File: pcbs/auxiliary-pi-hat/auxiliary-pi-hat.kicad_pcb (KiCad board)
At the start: 2 copper layers, 85 x 56 mm, 29 parts, among them J1 Conn_01x02, J10 Conn_01x03, J11 Conn_01x03, J2 Raspberry Pi - Hat Template -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, J3 Conn_01x03, J4 Conn_01x03, J5 Conn_01x03, J7 Conn_01x04, J8 Conn_02x04_Odd_Even, J9 Conn_01x05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

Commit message: PCB update
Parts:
- added JP1: Jumper_3_Open, Jumper:SolderJumper-3_P1.3mm_Open_Pad1.0x1.5mm, F.Cu at (145.2, 81.0)
- added R10: 10k, Resistor_SMD:R_1206_3216Metric, F.Cu at (162.2, 61.0)
- added R11: 10k, Resistor_SMD:R_1206_3216Metric, F.Cu at (165.8, 61.0)
- added R12: 10k, Resistor_SMD:R_1206_3216Metric, F.Cu at (169.0, 61.0)
- J2: footprint General:Raspberry Pi - Hat Template - Full Size -> sbcs:Raspberry Pi - Hat Template - Full Size Extended
- MOD1: footprint General:BNO055 Module -> general:BNO055 Module; moved to B.Cu
- R4: value R_Small_US -> 10k
- U1: footprint MCU_Modules:YAAJ_WeAct_BlackPill_2 -> mcus:Blackpill WeAct
- moved G*** 132.1 mm to (97.2, 75.5)
- moved LS1 83.5 mm to (98.8, 92.5), turned to 0 degrees
- moved SW1 72.0 mm to (90.8, 89.0), turned to -90 degrees
- moved Q3 62.0 mm to (107.5, 88.8)
- moved U2 61.1 mm to (132.9, 60.9), turned to -90 degrees
- moved R4 51.2 mm to (159.0, 61.0)
- moved R1 46.1 mm to (127.5, 64.0), turned to 180 degrees
- moved J11 44.2 mm to (99.0, 59.2), turned to 180 degrees
- moved J1 42.0 mm to (88.2, 55.8), turned to -90 degrees
- moved J3 32.8 mm to (165.0, 98.5)
- moved R2 31.9 mm to (139.0, 81.2), turned to 0 degrees
- moved R3 30.7 mm to (162.5, 89.5)
- moved R5 28.8 mm to (162.5, 74.0), turned to 90 degrees
- moved R6 28.4 mm to (162.5, 79.5)
- moved J10 26.5 mm to (171.5, 98.5)
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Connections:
- J2 pad 17: unconnected-(J2-3.3v-Pad17) -> 3v3-RPI
- J2 pad 32: BUZZER -> BUZZER_RPI
- J4 pad 2: GPIO-2 -> AUX
- R2 pad 2: BUZZER -> Net-(JP1-C)
- R4 pad 1: NEO-1 -> GPIO-20
- R4 pad 2: Net-(J4-Pin_2) -> 3v3-RPI
- U1 pad 16: BTN-1 -> AUX
- U1 pad 17: unconnected-(U1-PB9-Pad17) -> BUZZER_MCU
- U1 pad 23: unconnected-(U1-PC14-Pad23) -> BTN-1
- U1 pad 27: RC-PWM-0 -> unconnected-(U1-PA1-Pad27)
- U1 pad 5: unconnected-(U1-PA8-Pad5) -> RC-PWM-0
- U2 pad 5: +5V -> +3.3V
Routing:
- net +3.3V: track 0.00 -> 210.4 mm, vias 0 -> 4
- net +5V: track 0.00 -> 202.6 mm, vias 0 -> 2
- net GND: track 0.00 -> 108.0 mm, vias 0 -> 7
- net TFT-CS: track 0.00 -> 89.2 mm, vias 0 -> 2
- net TFT-RESET: track 0.00 -> 84.2 mm, vias 0 -> 2
- net TFT-DC: track 0.00 -> 80.4 mm, vias 0 -> 2
- net TFT-MOSI: track 0.00 -> 76.4 mm, vias 0 -> 2
- net BTN-1: track 0.00 -> 75.0 mm
- net TFT-SCK: track 0.00 -> 70.4 mm, vias 0 -> 2
- net SDA: track 0.00 -> 65.7 mm, vias 0 -> 2
- net SCL: track 0.00 -> 65.6 mm, vias 0 -> 2
- net NEO-0: track 0.00 -> 64.7 mm, vias 0 -> 2
- net RC-PWM-0: track 0.00 -> 55.7 mm
- net NEO-1: track 0.00 -> 54.5 mm
- net 3v3-RPI: track 0.00 -> 53.9 mm
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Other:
- board size 85 x 56 mm -> 93 x 56 mm
- board text added: "CONTACTS"
- board text added: "ElectroPup Auxiliary Pi Hat metaphasiclabs.com 10/2024"
- board text added: "SKY"
- board text added: "STM32 Blackpill"
- board text removed: "BTN0"
- board text removed: "BTN1"
- board text removed: "ElectroPup Auxiliary Pi Hat metaphasiclabs.com 09/2024"
- board text removed: "STM32 Bluepill/Blackpill"

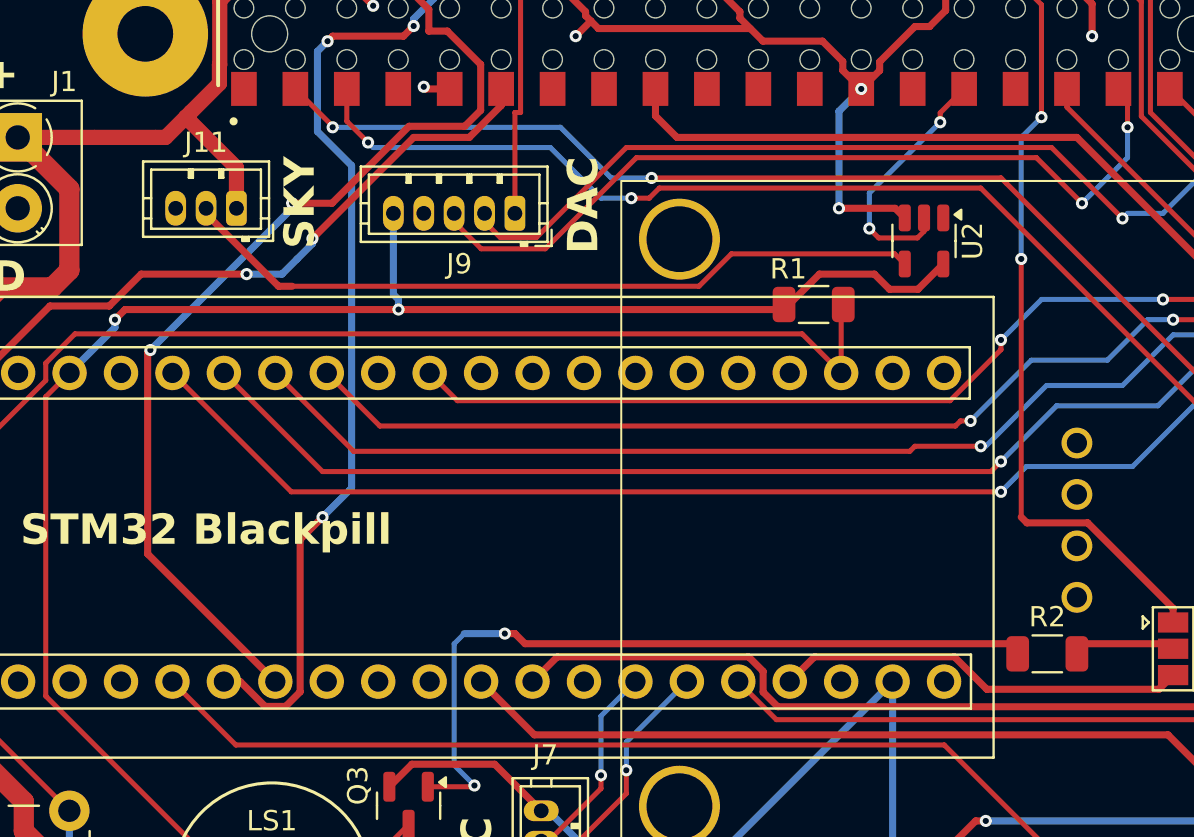
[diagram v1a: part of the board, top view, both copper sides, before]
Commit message: plot.py update to handle no gamepad connected
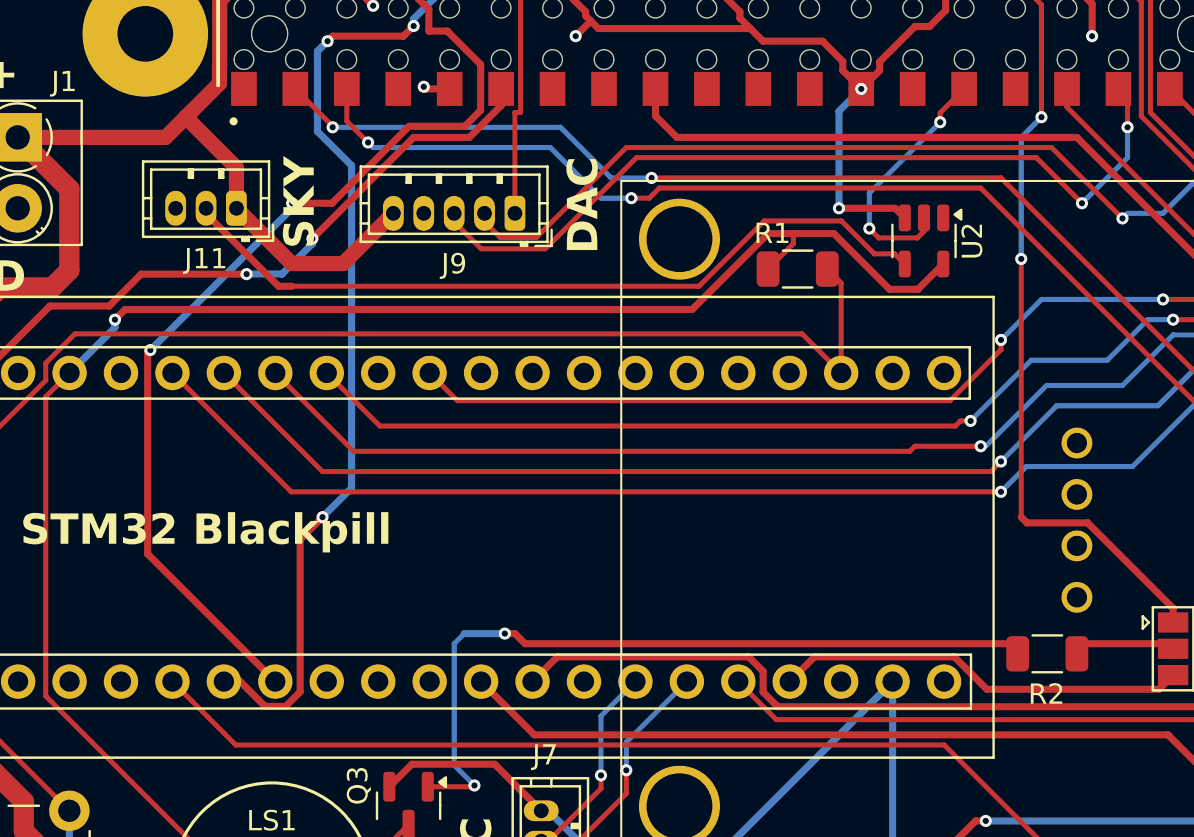
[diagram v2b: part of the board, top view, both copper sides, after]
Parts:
- moved R1 1.92 mm to (126.7, 62.2)
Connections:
- J9 pad 5: +3.3V -> +5V
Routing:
- net +5V: track 202.6 -> 212.5 mm
- net BTN-1: track 75.0 -> 77.3 mm
- net Net-(J11-Pin_2): track 37.4 -> 38.7 mm
- net +3.3V: track 210.4 -> 209.4 mm, vias 4 -> 3
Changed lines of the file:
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@@
 		(tags "resistor")
 		(property "Reference" "R2"
-			(at 0 -1.82 360)
+			(at -0.0375 2 360)
 			(layer "F.SilkS")
 			(effects
@@
 		(tags "connector JST ZH vertical")
 		(property "Reference" "J9"
-			(at 2.75 -2.5 180)
+			(at 3 -2.5 180)
 			(layer "F.SilkS")
 			(effects
@@
 			(layers "*.Cu" "*.Mask")
 			(remove_unused_layers no)
-			(net 14 "+3.3V")
+			(net 7 "+5V")
 			(pinfunction "Pin_5")
 			(pintype "passive")
@@
 		(tags "connector JST ZH vertical")
 		(property "Reference" "J11"
-			(at 1.5 3.25 360)
+			(at 1.5 -2.5 360)
 			(layer "F.SilkS")
 			(effects
@@
 	(footprint "Resistor_SMD:R_1206_3216Metric"
 		(layer "F.Cu")
-		(at 127.5 64 180)
+		(at 126.7125 62.25 180)
 		(descr "Resistor SMD 1206 (3216 Metric), square (rectangular) end terminal, IPC_7351 nominal, (Body size source: IPC-SM-782 page 72, https://www.pcb-3d.com/wordpress/wp-content/uploads/ipc-sm-782a_amendment_1_and_2.pdf), generated with kicad-footprint-generator")
 		(tags "resistor")
@@
 	)
 	(segment
+		(start 104.269925 61.980075)
+		(end 101.730075 61.980075)
+		(width 0.75)
+		(layer "F.Cu")
+		(net 7)
+	)
+	(segment
 		(start 88.5 90)
 		(end 88.5 88.54)
@@
 	)
 	(segment
+		(start 101.730075 61.980075)
+		(end 99 59.25)
+		(width 0.75)
+		(layer "F.Cu")
+		(net 7)
+	)
+	(segment
+		(start 106.75 59.5)
+		(end 104.269925 61.980075)
+		(width 0.75)
+		(layer "F.Cu")
+		(net 7)
+	)
+	(segment
 		(start 90.75 58.3)
 		(end 88.2 55.75)
@@
 	)
 	(segment
-		(start 127.7875 62.5)
-		(end 126.0375 64.25)
-		(width 0.35)
-		(layer "F.Cu")
-		(net 14)
-	)
-	(segment
 		(start 163.75 88.75)
 		(end 163 89.5)
@@
 	)
 	(segment
-		(start 131.25 63.25)
-		(end 130.5 62.5)
-		(width 0.35)
-		(layer "F.Cu")
-		(net 14)
-	)
-	(segment
 		(start 163.75 83.8625)
 		(end 163.75 88.75)
@@
 	)
 	(segment
-		(start 126.0375 64.25)
-		(end 107 64.25)
-		(width 0.35)
-		(layer "F.Cu")
-		(net 14)
-	)
-	(segment
 		(start 163.9625 83.05)
 		(end 163.45 83.5625)
@@
 	)
 	(segment
-		(start 93.5 64.25)
-		(end 93 64.75)
-		(width 0.35)
-		(layer "F.Cu")
-		(net 14)
-	)
-	(segment
 		(start 169.4625 74.9625)
 		(end 169.025 74.525)
@@
 	)
 	(segment
-		(start 130.5 62.5)
-		(end 127.7875 62.5)
+		(start 93.5 64.25)
+		(end 93 64.75)
 		(width 0.35)
 		(layer "F.Cu")
@@
 	)
 	(segment
+		(start 125.25 62.25)
+		(end 126.5 61)
+		(width 0.25)
+		(layer "F.Cu")
+		(net 14)
+	)
+	(segment
 		(start 175.137 67.147)
 		(end 175.137 82.653)
@@
 	)
 	(segment
+		(start 133.9 62)
+		(end 132.65 63.25)
+		(width 0.35)
+		(layer "F.Cu")
+		(net 14)
+	)
+	(segment
+		(start 132.65 63.25)
+		(end 131.25 63.25)
+		(width 0.35)
+		(layer "F.Cu")
+		(net 14)
+	)
+	(segment
 		(start 160.5 89.5)
 		(end 152.5 89.5)
@@
 	)
 	(segment
+		(start 126.5 61)
+		(end 126.5 60.5)
+		(width 0.25)
+		(layer "F.Cu")
+		(net 14)
+	)
+	(segment
 		(start 169.025 74.525)
 		(end 166.975 74.525)
@@
 	)
 	(segment
-		(start 132.65 63.25)
-		(end 131.25 63.25)
+		(start 131.25 63.25)
+		(end 128.5 60.5)
 		(width 0.35)
 		(layer "F.Cu")
@@
 	)
 	(segment
-		(start 174 66.01)
-		(end 175.137 67.147)
+		(start 126.5 60.5)
+		(end 125.25 60.5)
 		(width 0.35)
 		(layer "F.Cu")
@@
 	)
 	(segment
-		(start 133.9 62)
-		(end 132.65 63.25)
+		(start 174 66.01)
+		(end 175.137 67.147)
 		(width 0.35)
 		(layer "F.Cu")
@@
 	)
 	(segment
+		(start 125.25 60.5)
+		(end 121.5 64.25)
+		(width 0.35)
+		(layer "F.Cu")
+		(net 14)
+	)
+	(segment
 		(start 159.365 98.5)
 		(end 158.5 98.5)
@@
 	)
 	(segment
-		(start 107 64.25)
+		(start 121.5 64.25)
 		(end 93.5 64.25)
 		(width 0.35)
@@
 	)
 	(segment
+		(start 128.5 60.5)
+		(end 126.5 60.5)
+		(width 0.35)
+		(layer "F.Cu")
+		(net 14)
+	)
+	(segment
 		(start 163 89.5)
 		(end 160.5 89.5)
@@
 		(net 14)
 	)
-	(via
-		(at 107 64.25)
-		(size 0.6)
-		(drill 0.3)
-		(layers "F.Cu" "B.Cu")
-		(net 14)
-	)
 	(segment
 		(start 152.5 89.5)
@@
 	)
 	(segment
-		(start 107 63.75)
-		(end 106.75 63.5)
-		(width 0.35)
-		(layer "B.Cu")
-		(net 14)
-	)
-	(segment
-		(start 106.75 63.5)
-		(end 106.75 59.5)
-		(width 0.35)
-		(layer "B.Cu")
-		(net 14)
-	)
-	(segment
-		(start 107 64.25)
-		(end 107 63.75)
-		(width 0.35)
-		(layer "B.Cu")
-		(net 14)
-	)
-	(segment
 		(start 93 64.75)
 		(end 93 65.14)
@@
 	)
 	(segment
-		(start 90.75 89)
-		(end 87.045 85.295)
+		(start 128.86 62.935)
+		(end 128.175 62.25)
 		(width 0.25)
 		(layer "F.Cu")
@@
 	)
 	(segment
-		(start 87.045 85.295)
-		(end 87.045 70.29)
+		(start 128.86 67.38)
+		(end 128.86 62.935)
 		(width 0.25)
 		(layer "F.Cu")
@@
 	)
 	(segment
-		(start 91.028299 65.45)
-		(end 126.93 65.45)
+		(start 90.75 89)
+		(end 87.045 85.295)
 		(width 0.25)
 		(layer "F.Cu")
@@
 	)
 	(segment
-		(start 128.86 64.3525)
-		(end 128.9625 64.25)
+		(start 87.045 85.295)
+		(end 87.045 70.29)
 		(width 0.25)
 		(layer "F.Cu")
@@
 	)
 	(segment
-		(start 128.86 67.38)
-		(end 128.86 64.3525)
+		(start 91.028299 65.45)
+		(end 126.93 65.45)
 		(width 0.25)
 		(layer "F.Cu")
@@
 	)
 	(segment
-		(start 97.5 59.52081)
-		(end 101.07919 63.1)
-		(width 0.35)
+		(start 128.875 59.875)
+		(end 125.063047 59.875)
+		(width 0.25)
 		(layer "F.Cu")
 		(net 58)
 	)
 	(segment
-		(start 97.5 59.25)
-		(end 97.5 59.52081)
-		(width 0.35)
+		(start 125.063047 59.875)
+		(end 121.838047 63.1)
+		(width 0.25)
 		(layer "F.Cu")
 		(net 58)
 	)
 	(segment
-		(start 101.75 63.1)
-		(end 101.5 63.1)
+		(start 130.5 61.5)
+		(end 128.875 59.875)
 		(width 0.25)
 		(layer "F.Cu")
@@
 	)
 	(segment
-		(start 121.838047 63.1)
-		(end 101.75 63.1)
+		(start 131.5 61.5)
+		(end 130.5 61.5)
 		(width 0.25)
 		(layer "F.Cu")
@@
 	)
 	(segment
-		(start 131.5 61.5)
-		(end 123.438047 61.5)
+		(start 97.5 59.52081)
+		(end 101.07919 63.1)
+		(width 0.35)
+		(layer "F.Cu")
+		(net 58)
+	)
+	(segment
+		(start 97.5 59.25)
+		(end 97.5 59.52081)
+		(width 0.35)
+		(layer "F.Cu")
+		(net 58)
+	)
+	(segment
+		(start 101.75 63.1)
+		(end 101.5 63.1)
 		(width 0.25)
 		(layer "F.Cu")
@@
 	)
 	(segment
-		(start 123.438047 61.5)
-		(end 121.838047 63.1)
+		(start 121.838047 63.1)
+		(end 101.75 63.1)
 		(width 0.25)
 		(layer "F.Cu")
